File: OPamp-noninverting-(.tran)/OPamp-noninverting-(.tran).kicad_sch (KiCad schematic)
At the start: 6 parts, among them U1 LM741

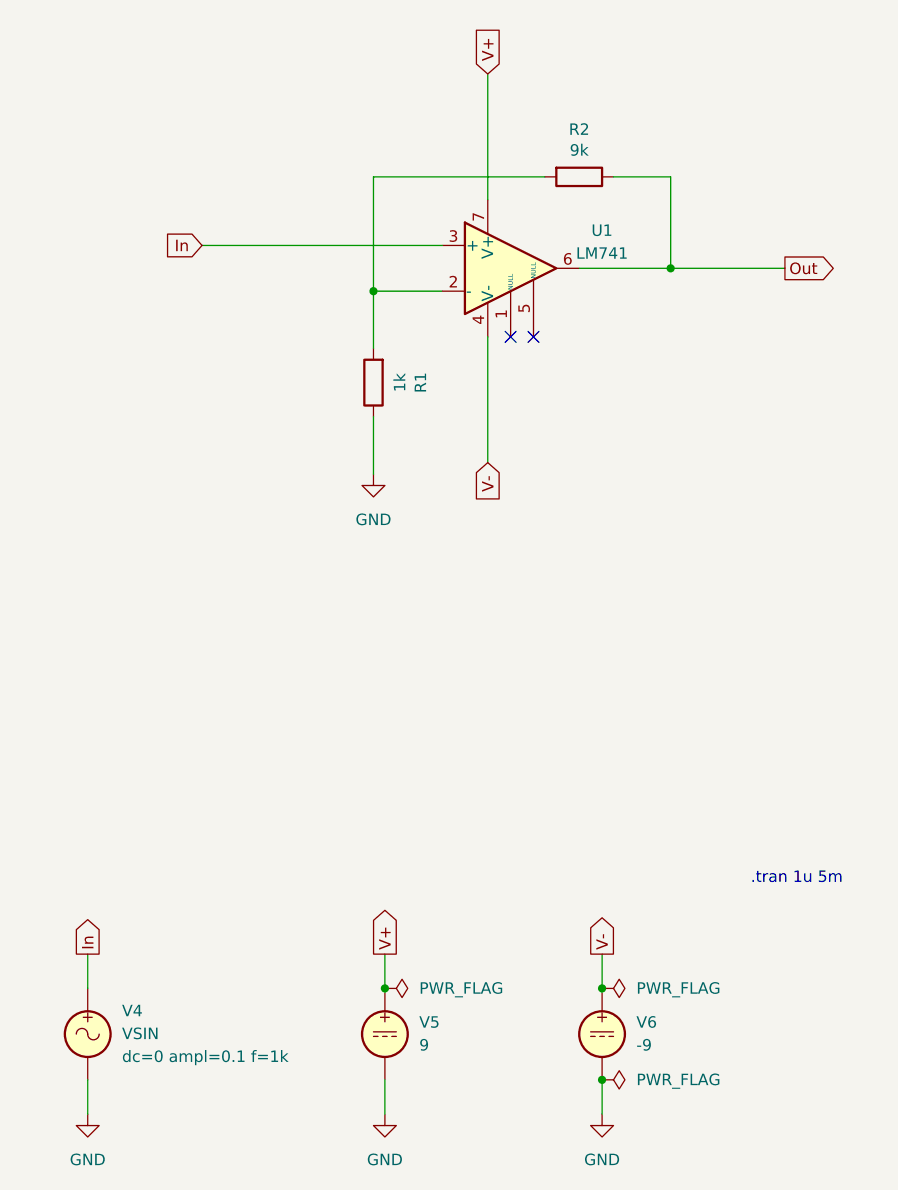
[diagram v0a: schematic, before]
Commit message: Updated all schematics and prepared for KiCad 8.0
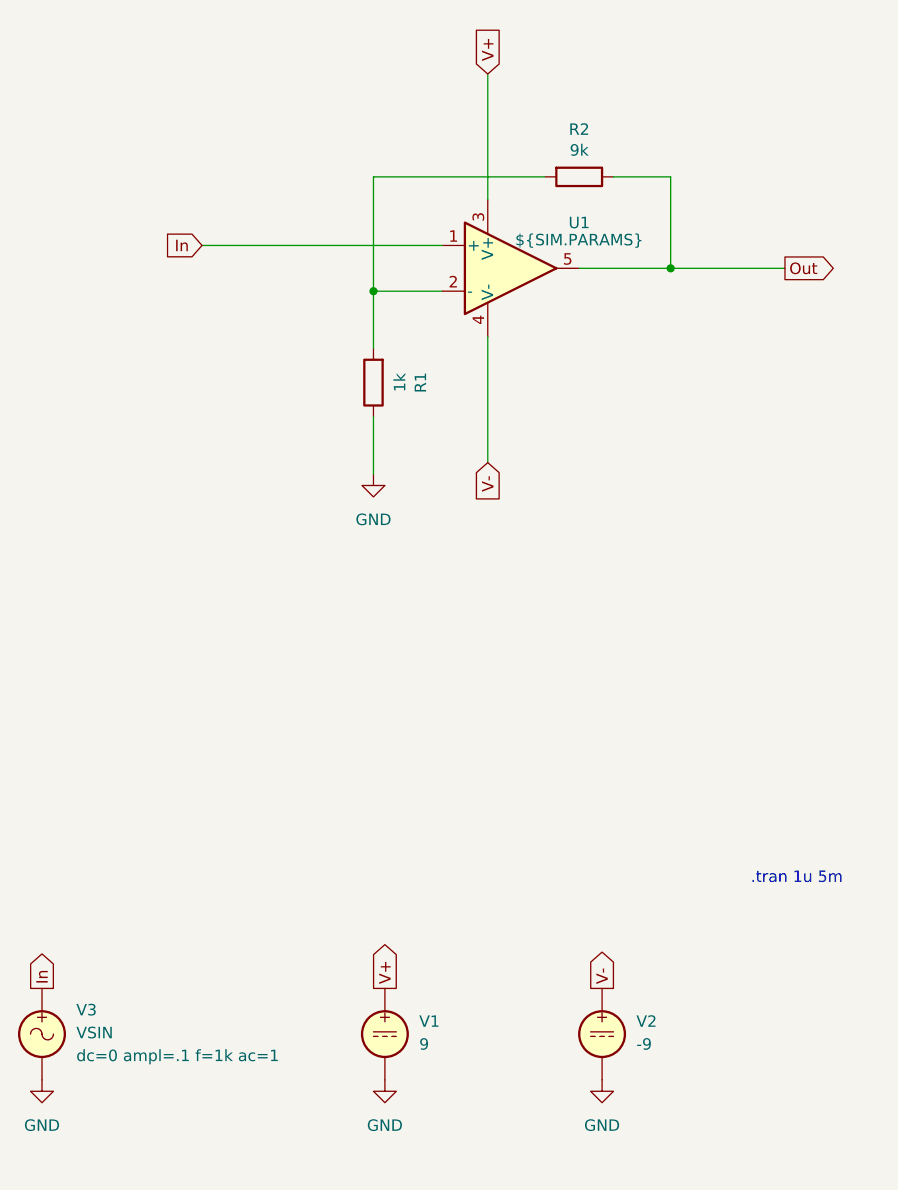
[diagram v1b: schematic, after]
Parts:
- removed U1: LM741, symbol Amplifier_Operational:LM741
- removed V4: VSIN, symbol Simulation_SPICE:VSIN
- removed V5: 9, symbol Simulation_SPICE:VDC
- removed V6: -9, symbol Simulation_SPICE:VDC
- added U1: ${SIM.PARAMS}, symbol Simulation_SPICE:OPAMP
- added V1: 9, symbol Simulation_SPICE:VDC
- added V2: -9, symbol Simulation_SPICE:VDC
- added V3: VSIN, symbol Simulation_SPICE:VSIN
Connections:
- net GND: now also V1.2, V2.2, V3.2
- net In: now also U1.1 (+), V3.1
- net Out: now also U1.5
- net V+: now also U1.3 (V+), V1.1
- net V-: now also U1.4 (V-), V2.1
- net at R1.2, R2.2: now also U1.2 (-)
- no-connect marks 2 -> 0
